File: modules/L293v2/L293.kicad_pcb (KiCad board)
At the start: 2 copper layers, 40.6 x 40.6 mm, 38 parts, among them J1 2, J10 11, J11 12, J12 13, J13 A0, J14 A1, J15 A2, J16 A3, J17 A4, J18 A5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

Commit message: Fix hash, add gerber
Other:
- rule solder_mask_min_width: 0.25 -> 0.1
- board text added: "3357b8"
- board text removed: "hash"

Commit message: Motor shield polishing
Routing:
- net (no net): track 8.26 -> 18.4 mm
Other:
- board text added: "+"

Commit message: Motor shield polishing
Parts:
- added C3: 0.1uF, Capacitor_SMD:C_0805_2012Metric_Pad1.15x1.40mm_HandSolder, B.Cu at (98.1, 60.6)
- added J24: Conn_01x01_Male, Connector_PinHeader_2.54mm:PinHeader_1x01_P2.54mm_Vertical, F.Cu at (97.8, 38.7)
- added J25: Conn_01x01_Male, Connector_PinHeader_2.54mm:PinHeader_1x01_P2.54mm_Vertical, F.Cu at (97.2, 57.8)
- added R3: 10k, Resistor_SMD:R_0805_2012Metric_Pad1.15x1.40mm_HandSolder, B.Cu at (106.4, 65.7)
- added R4: 50k, Resistor_SMD:R_0805_2012Metric_Pad1.15x1.40mm_HandSolder, B.Cu at (106.4, 61.3)
- moved C2 1.30 mm to (96.9, 54.6), turned to 0 degrees
- moved C4 0.64 mm to (102.2, 63.5)
- moved R2 0.39 mm to (112.1, 40.6)
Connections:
- J7 pad 1: /M1+ -> /M1-
- J8 pad 1: /M1- -> /M1+
- U1 pad 12: /M1+ -> /M1-
- U1 pad 13: /M1- -> /M1+
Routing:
- net Net-(C3-Pad2): track 0.00 -> 19.2 mm, vias 0 -> 1
- net Net-(J24-Pad1): track 2.14 -> 18.6 mm, vias 0 -> 1
- net /M1-: track 14.1 -> 11.2 mm
- net /M1+: track 11.2 -> 14.1 mm
- net VCC: track 87.7 -> 85.5 mm
- net Net-(C2-Pad2): track 30.8 -> 31.7 mm
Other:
- board text added: "87775e"
- board text added: "Bat Chk"
- board text added: "Rst"
- board text removed: "3357b8"

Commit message: Fix hash, add gerber
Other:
- board text added: "4d7577"
- board text removed: "87775e"

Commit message: Motor shield polishing
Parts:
- C3: moved to F.Cu
- moved C3 2.07 mm to (96.3, 59.7), turned to 0 degrees
- moved C4 0.45 mm to (102.6, 63.8)
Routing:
- net GND: track 112.8 -> 147.8 mm
- net Net-(C2-Pad2): track 31.7 -> 34.6 mm
- net Net-(C3-Pad2): track 19.2 -> 16.4 mm
- net VCC: track 85.5 -> 87.4 mm
- net (no net): track 18.4 -> 17.8 mm
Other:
- board text added: "1+"
- board text added: "1-"
- board text added: "13.11.2020"
- board text added: "1P"
- board text added: "2+"
- board text added: "2-"
- board text added: "2P"
- board text added: "La"
- board text removed: "12.11.2020"

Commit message: Fix hash, add gerber
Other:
- board text added: "974da1"
- board text removed: "4d7577"

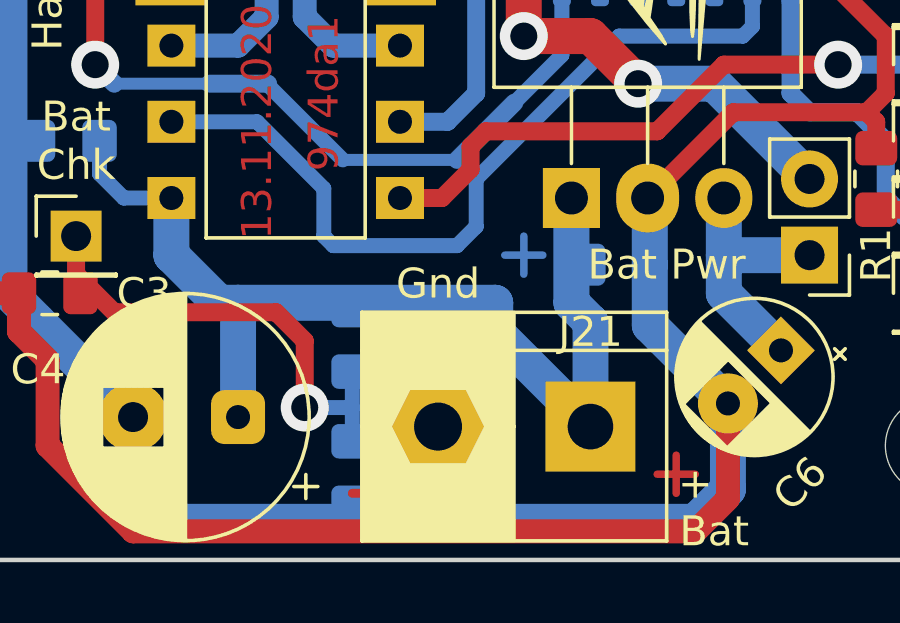
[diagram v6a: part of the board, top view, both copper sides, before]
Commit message: L293. Reverse polarity protection is added.
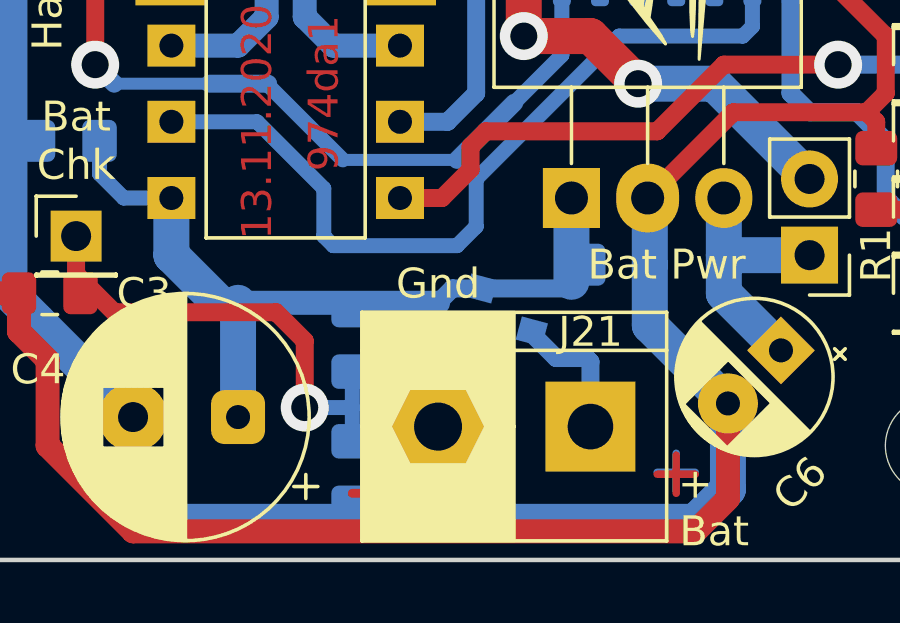
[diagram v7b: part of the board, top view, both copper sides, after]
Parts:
- added Q1: IRLML5203, Package_TO_SOT_SMD:SOT-23, B.Cu at (111.4, 60.7)
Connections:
- J21 pad 1: Net-(C2-Pad2) -> Net-(J21-Pad1)
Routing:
- net Net-(C2-Pad2): track 34.6 -> 26.9 mm
- net Net-(J21-Pad1): track 0.00 -> 4.33 mm
- net GND: track 147.8 -> 151.0 mm
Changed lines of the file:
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@@
     (thickness 1.6)
     (drawings 54)
-    (tracks 257)
+    (tracks 264)
     (zones 0)
-    (modules 43)
-    (nets 37)
+    (modules 44)
+    (nets 38)
   )
   (page A4 portrait)
@@
   )
   (setup
-    (last_trace_width 0.25)
+    (last_trace_width 0.6)
     (user_trace_width 0.4)
     (user_trace_width 0.5)
@@
   (net 35 "Net-(C3-Pad2)")
   (net 36 "Net-(J24-Pad1)")
+  (net 37 "Net-(J21-Pad1)")
   (net_class Default "Это класс цепей по умолчанию."
     (clearance 0.2)
@@
     (add_net "Net-(J17-Pad1)")
     (add_net "Net-(J18-Pad1)")
+    (add_net "Net-(J21-Pad1)")
     (add_net "Net-(J22-Pad1)")
     (add_net "Net-(J22-Pad2)")
@@
     )
     (pad 1 thru_hole rect (at 0 0 180) (size 3 3) (drill 1.52) (layers *.Cu *.Mask)
-      (net 14 "Net-(C2-Pad2)"))
+      (net 37 "Net-(J21-Pad1)"))
     (pad 2 thru_hole circle (at 5.08 0 180) (size 3.5 3.5) (drill 1.6) (layers *.Cu *.Mask)
       (net 13 GND))
@@
     )
   )
+  (module Package_TO_SOT_SMD:SOT-23 (layer B.Cu)
+    (at 111.379 60.706 345)
+    (descr "SOT-23, Standard")
+    (tags SOT-23)
+    (attr smd)
+    (fp_text reference Q1 (at 0 2.5 165) (layer B.SilkS)
+      (effects (font (size 1 1) (thickness 0.15)) (justify mirror))
+    )
+    (fp_text value IRLML5203 (at 0 -2.5 165) (layer B.Fab)
+      (effects (font (size 1 1) (thickness 0.15)) (justify mirror))
+    )
+    (fp_line (start -0.7 0.95) (end -0.7 -1.5) (layer B.Fab) (width 0.1))
+    (fp_line (start -0.15 1.52) (end 0.7 1.52) (layer B.Fab) (width 0.1))
+    (fp_line (start -0.7 0.95) (end -0.15 1.52) (layer B.Fab) (width 0.1))
+    (fp_line (start 0.7 1.52) (end 0.7 -1.52) (layer B.Fab) (width 0.1))
+    (fp_line (start -0.7 -1.52) (end 0.7 -1.52) (layer B.Fab) (width 0.1))
+    (fp_line (start 0.76 -1.58) (end 0.76 -0.65) (layer B.SilkS) (width 0.12))
+    (fp_line (start 0.76 1.58) (end 0.76 0.65) (layer B.SilkS) (width 0.12))
+    (fp_line (start -1.7 1.75) (end 1.7 1.75) (layer B.CrtYd) (width 0.05))
+    (fp_line (start 1.7 1.75) (end 1.7 -1.75) (layer B.CrtYd) (width 0.05))
+    (fp_line (start 1.7 -1.75) (end -1.7 -1.75) (layer B.CrtYd) (width 0.05))
+    (fp_line (start -1.7 -1.75) (end -1.7 1.75) (layer B.CrtYd) (width 0.05))
+    (fp_line (start 0.76 1.58) (end -1.4 1.58) (layer B.SilkS) (width 0.12))
+    (fp_line (start 0.76 -1.58) (end -0.7 -1.58) (layer B.SilkS) (width 0.12))
+    (fp_text user %R (at 0 0 255) (layer B.Fab)
+      (effects (font (size 0.5 0.5) (thickness 0.075)) (justify mirror))
+    )
+    (pad 1 smd rect (at -1 0.95 345) (size 0.9 0.8) (layers B.Cu B.Paste B.Mask)
+      (net 13 GND))
+    (pad 2 smd rect (at -1 -0.95 345) (size 0.9 0.8) (layers B.Cu B.Paste B.Mask)
+      (net 14 "Net-(C2-Pad2)"))
+    (pad 3 smd rect (at 1 0 345) (size 0.9 0.8) (layers B.Cu B.Paste B.Mask)
+      (net 37 "Net-(J21-Pad1)"))
+    (model ${KISYS3DMOD}/Package_TO_SOT_SMD.3dshapes/SOT-23.wrl
+      (at (xyz 0 0 0))
+      (scale (xyz 1 1 1))
+      (rotate (xyz 0 0 0))
+    )
+  )
   (gr_text 2+ (at 127.9525 39.37) (layer B.SilkS)
     (effects (font (size 1 1) (thickness 0.15)) (justify mirror))
@@
   (segment (start 89.535 36.83) (end 90.805 36.83) (width 0.25) (layer F.Cu) (net 0))
   (segment (start 90.17 36.195) (end 90.17 37.465) (width 0.25) (layer F.Cu) (net 0))
-  (segment (start 112.0775 59.055) (end 112.0775 57.785) (width 0.25) (layer B.Cu) (net 0))
-  (segment (start 111.4425 58.42) (end 112.7125 58.42) (width 0.25) (layer B.Cu) (net 0))
+  (segment (start 117.1575 66.294) (end 117.1575 65.024) (width 0.25) (layer B.Cu) (net 0))
+  (segment (start 116.5225 65.659) (end 117.7925 65.659) (width 0.25) (layer B.Cu) (net 0))
   (segment (start 90.17 37.465) (end 90.17 36.195) (width 0.25) (layer B.Cu) (net 0))
   (segment (start 89.535 36.83) (end 90.805 36.83) (width 0.25) (layer B.Cu) (net 0))
@@
   (segment (start 96.2025 61.9125) (end 96.2025 64.77) (width 0.8) (layer F.Cu) (net 13))
   (segment (start 95.25 59.69) (end 92.71 59.69) (width 0.8) (layer F.Cu) (net 13))
+  (segment (start 110.167196 61.36481) (end 110.167196 62.298804) (width 0.6) (layer B.Cu) (net 13))
+  (segment (start 109.22 63.246) (end 109.22 64.135) (width 0.6) (layer B.Cu) (net 13))
+  (segment (start 110.167196 62.298804) (end 109.22 63.246) (width 0.6) (layer B.Cu) (net 13))
   (segment (start 113.665 58.7375) (end 114.3 58.7375) (width 0.8) (layer B.Cu) (net 14))
-  (segment (start 113.665 56.515) (end 113.665 60.0075) (width 1.2) (layer B.Cu) (net 14))
-  (segment (start 114.3 60.6425) (end 114.3 64.135) (width 1.2) (layer B.Cu) (net 14))
-  (segment (start 113.665 60.0075) (end 114.3 60.6425) (width 1.2) (layer B.Cu) (net 14))
   (segment (start 102.5525 63.5) (end 102.5525 60.0075) (width 1.2) (layer B.Cu) (net 14))
   (segment (start 97.935 55.7075) (end 97.935 54.61) (width 0.5) (layer B.Cu) (net 14))
@@
   (segment (start 100.33 58.42) (end 101.9175 60.0075) (width 1.2) (layer B.Cu) (net 14))
   (segment (start 100.33 56.515) (end 100.33 58.42) (width 1.2) (layer B.Cu) (net 14))
-  (segment (start 111.125 60.96) (end 114.3 64.135) (width 1.2) (layer B.Cu) (net 14))
-  (segment (start 111.125 60.0075) (end 111.125 60.96) (width 1.2) (layer B.Cu) (net 14))
-  (segment (start 101.9175 60.0075) (end 111.125 60.0075) (width 1.2) (layer B.Cu) (net 14))
+  (segment (start 101.9175 60.0075) (end 109.22 60.0075) (width 0.8) (layer B.Cu) (net 14))
+  (segment (start 109.697949 59.529551) (end 109.22 60.0075) (width 0.6) (layer B.Cu) (net 14))
+  (segment (start 110.658952 59.529551) (end 109.697949 59.529551) (width 0.6) (layer B.Cu) (net 14))
+  (segment (start 110.658952 59.529551) (end 113.444449 59.529551) (width 0.6) (layer B.Cu) (net 14))
+  (segment (start 113.444449 59.529551) (end 113.665 59.309) (width 0.6) (layer B.Cu) (net 14))
+  (segment (start 113.665 56.515) (end 113.665 59.309) (width 1.2) (layer B.Cu) (net 14))
   (segment (start 103.505 50.4825) (end 103.505 35.56) (width 0.8) (layer B.Cu) (net 15))
   (segment (start 103.505 35.56) (end 105.41 33.655) (width 0.8) (layer B.Cu) (net 15))
@@
   (segment (start 111.515 41.665) (end 110.1725 40.3225) (width 0.5) (layer B.Cu) (net 36))
   (segment (start 112.0775 41.665) (end 111.515 41.665) (width 0.5) (layer B.Cu) (net 36))
+  (segment (start 112.467107 61.159107) (end 113.157 61.849) (width 0.6) (layer B.Cu) (net 37))
+  (segment (start 113.157 61.849) (end 114.173 61.849) (width 0.6) (layer B.Cu) (net 37))
+  (segment (start 114.3 61.976) (end 114.3 64.135) (width 0.6) (layer B.Cu) (net 37))
+  (segment (start 114.173 61.849) (end 114.3 61.976) (width 0.6) (layer B.Cu) (net 37))
 )

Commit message: Fix hash, add gerber
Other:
- board text added: "28.11.2020"
- board text added: "8ea343"
- board text removed: "13.11.2020"
- board text removed: "974da1"
